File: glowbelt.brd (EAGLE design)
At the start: 40.3 x 24.8 mm, 13 parts, among them IC1 TINY10S

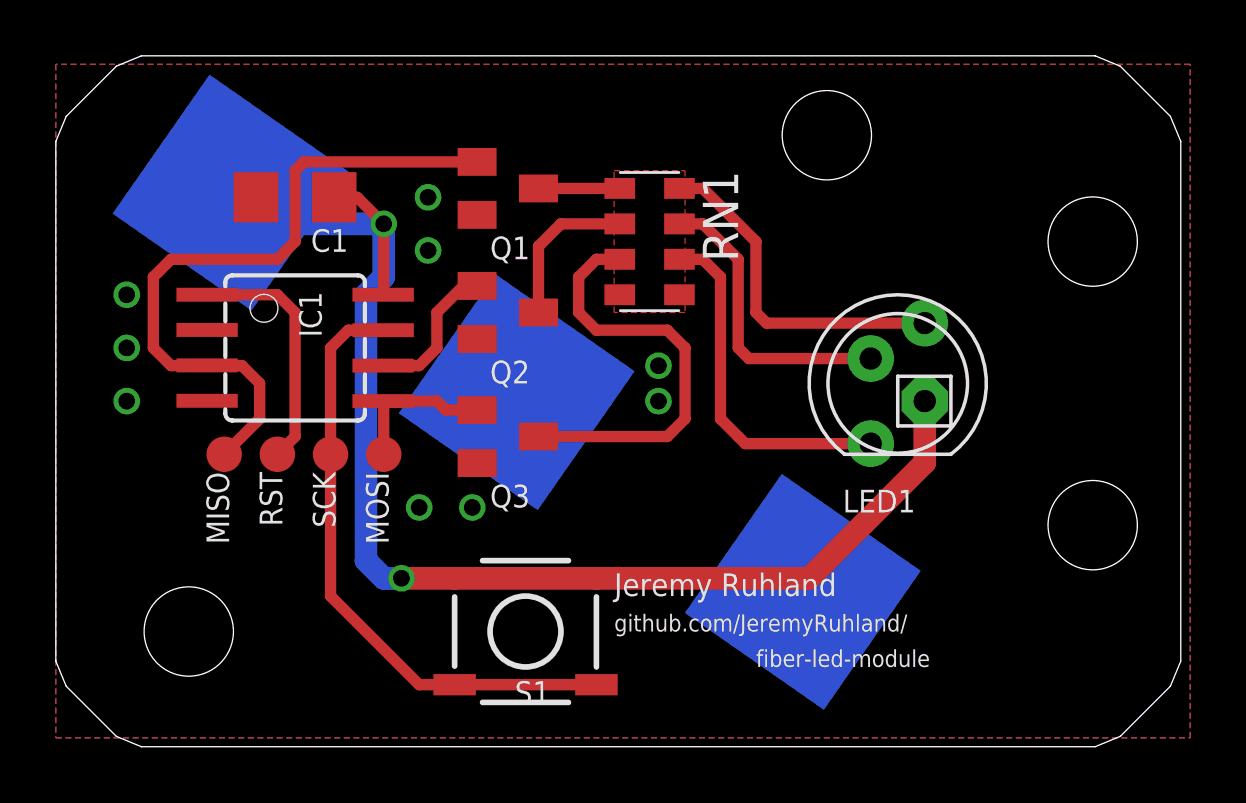
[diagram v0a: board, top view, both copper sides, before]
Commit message: increased spacing for a couple vias
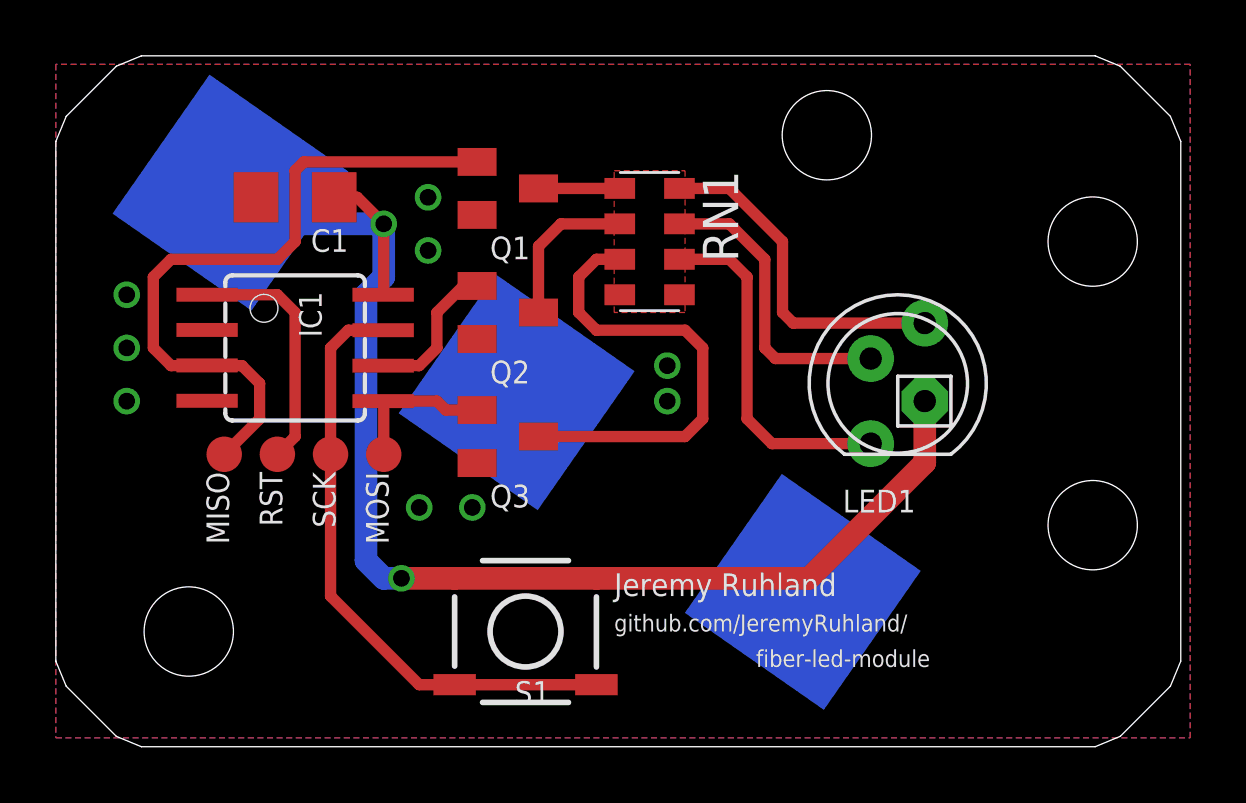
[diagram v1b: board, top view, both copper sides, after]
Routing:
- net N$4: track 15.4 -> 16.7 mm
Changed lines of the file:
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@@
 <via x="13.6525" y="19.3675" extent="1-16" drill="0.6"/>
 <via x="13.6525" y="17.4625" extent="1-16" drill="0.6"/>
-<via x="21.9075" y="12.065" extent="1-16" drill="0.6"/>
-<via x="21.9075" y="13.335" extent="1-16" drill="0.6"/>
+<via x="22.225" y="12.065" extent="1-16" drill="0.6"/>
+<via x="22.225" y="13.335" extent="1-16" drill="0.6"/>
 <via x="15.24" y="8.255" extent="1-16" drill="0.6"/>
 <via x="13.335" y="8.255" extent="1-16" drill="0.6"/>
@@
 <contactref element="Q3" pad="3"/>
 <contactref element="RN1" pad="3"/>
-<wire x1="17.61" y1="10.795" x2="22.225" y2="10.795" width="0.4064" layer="1"/>
-<wire x1="22.225" y1="10.795" x2="22.86" y2="11.43" width="0.4064" layer="1"/>
-<wire x1="22.86" y1="11.43" x2="22.86" y2="13.97" width="0.4064" layer="1"/>
-<wire x1="22.86" y1="13.97" x2="22.225" y2="14.605" width="0.4064" layer="1"/>
-<wire x1="22.225" y1="14.605" x2="19.685" y2="14.605" width="0.4064" layer="1"/>
+<wire x1="17.61" y1="10.795" x2="22.86" y2="10.795" width="0.4064" layer="1"/>
+<wire x1="22.86" y1="10.795" x2="23.495" y2="11.43" width="0.4064" layer="1"/>
+<wire x1="23.495" y1="11.43" x2="23.495" y2="13.97" width="0.4064" layer="1"/>
+<wire x1="23.495" y1="13.97" x2="22.86" y2="14.605" width="0.4064" layer="1"/>
+<wire x1="22.86" y1="14.605" x2="19.685" y2="14.605" width="0.4064" layer="1"/>
 <wire x1="19.685" y1="14.605" x2="19.05" y2="15.24" width="0.4064" layer="1"/>
 <wire x1="19.05" y1="15.24" x2="19.05" y2="16.51" width="0.4064" layer="1"/>
@@
 <contactref element="RN1" pad="7"/>
 <contactref element="LED1" pad="3"/>
-<wire x1="29.5116" y1="13.589" x2="25.146" y2="13.589" width="0.4064" layer="1"/>
-<wire x1="25.146" y1="13.589" x2="24.765" y2="13.97" width="0.4064" layer="1"/>
-<wire x1="24.765" y1="13.97" x2="24.765" y2="17.145" width="0.4064" layer="1"/>
-<wire x1="24.765" y1="17.145" x2="23.495" y2="18.415" width="0.4064" layer="1"/>
-<wire x1="23.495" y1="18.415" x2="22.66" y2="18.415" width="0.4064" layer="1"/>
+<wire x1="29.5116" y1="13.589" x2="26.0985" y2="13.589" width="0.4064" layer="1"/>
+<wire x1="26.0985" y1="13.589" x2="25.7175" y2="13.97" width="0.4064" layer="1"/>
+<wire x1="25.7175" y1="13.97" x2="25.7175" y2="17.145" width="0.4064" layer="1"/>
+<wire x1="25.7175" y1="17.145" x2="24.4475" y2="18.415" width="0.4064" layer="1"/>
+<wire x1="24.4475" y1="18.415" x2="22.66" y2="18.415" width="0.4064" layer="1"/>
 </signal>
 <signal name="N$6">
 <contactref element="RN1" pad="8"/>
 <contactref element="LED1" pad="4"/>
-<wire x1="31.4484" y1="14.859" x2="25.781" y2="14.859" width="0.4064" layer="1"/>
-<wire x1="25.781" y1="14.859" x2="25.4" y2="15.24" width="0.4064" layer="1"/>
-<wire x1="25.4" y1="15.24" x2="25.4" y2="17.78" width="0.4064" layer="1"/>
-<wire x1="25.4" y1="17.78" x2="23.495" y2="19.685" width="0.4064" layer="1"/>
-<wire x1="23.495" y1="19.685" x2="22.66" y2="19.685" width="0.4064" layer="1"/>
+<wire x1="31.4484" y1="14.859" x2="26.7335" y2="14.859" width="0.4064" layer="1"/>
+<wire x1="26.7335" y1="14.859" x2="26.3525" y2="15.24" width="0.4064" layer="1"/>
+<wire x1="26.3525" y1="15.24" x2="26.3525" y2="17.78" width="0.4064" layer="1"/>
+<wire x1="26.3525" y1="17.78" x2="24.4475" y2="19.685" width="0.4064" layer="1"/>
+<wire x1="24.4475" y1="19.685" x2="22.66" y2="19.685" width="0.4064" layer="1"/>
 </signal>
 <signal name="N$7">
 <contactref element="RN1" pad="6"/>
 <contactref element="LED1" pad="1"/>
-<wire x1="22.66" y1="17.145" x2="23.495" y2="17.145" width="0.4064" layer="1"/>
-<wire x1="23.495" y1="17.145" x2="24.13" y2="16.51" width="0.4064" layer="1"/>
-<wire x1="24.13" y1="16.51" x2="24.13" y2="11.43" width="0.4064" layer="1"/>
-<wire x1="24.13" y1="11.43" x2="24.765" y2="10.795" width="0.4064" layer="1"/>
-<wire x1="29.5116" y1="10.541" x2="25.019" y2="10.541" width="0.4064" layer="1"/>
-<wire x1="25.019" y1="10.541" x2="24.765" y2="10.795" width="0.4064" layer="1"/>
+<wire x1="22.66" y1="17.145" x2="24.4475" y2="17.145" width="0.4064" layer="1"/>
+<wire x1="24.4475" y1="17.145" x2="25.0825" y2="16.51" width="0.4064" layer="1"/>
+<wire x1="25.0825" y1="16.51" x2="25.0825" y2="11.43" width="0.4064" layer="1"/>
+<wire x1="25.0825" y1="11.43" x2="25.9715" y2="10.541" width="0.4064" layer="1"/>
+<wire x1="29.5116" y1="10.541" x2="25.9715" y2="10.541" width="0.4064" layer="1"/>
 </signal>
 <signal name="N$8">
